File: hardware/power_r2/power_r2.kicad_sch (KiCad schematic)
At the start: 11 parts

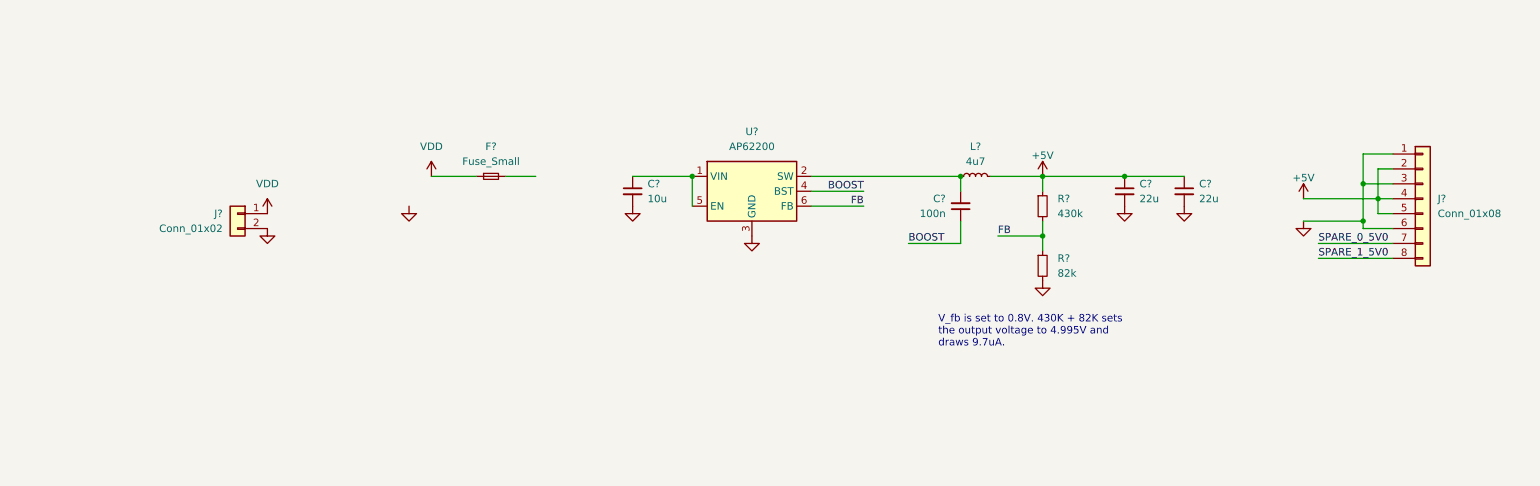
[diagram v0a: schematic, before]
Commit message: Display board layout is now 95% complete, the number of caps on the board might need some further tweaking and there are also some gaps where a few more LEDs could fit. Additionally I've decided to provide the option to use the hinges as the ground connection allowing more +5V channels on the FFC connectors which should mean more current carrying capacity. The new power board schematic has had some changes, namely the vreg has changed and so have some of the passives around it, more input protect has been added, a MOV for over voltage protection and an NMOS for reverse pol. Looking at the new vreg the power dissipation before it cooks itself (~1.1W) isn't great but it's enough for about 2.5A (at around 93% eff.) for the LEDs which hasn't usually been the bottleneck (looking at you 9V batteries). This means we're expecting around 1.8A peak input current at a Vin of 7V and need to size the fuze around that as much more current and the vreg is cooked. Might look into a over voltage shutout circuit if it seems like we're blowing fuses too often.
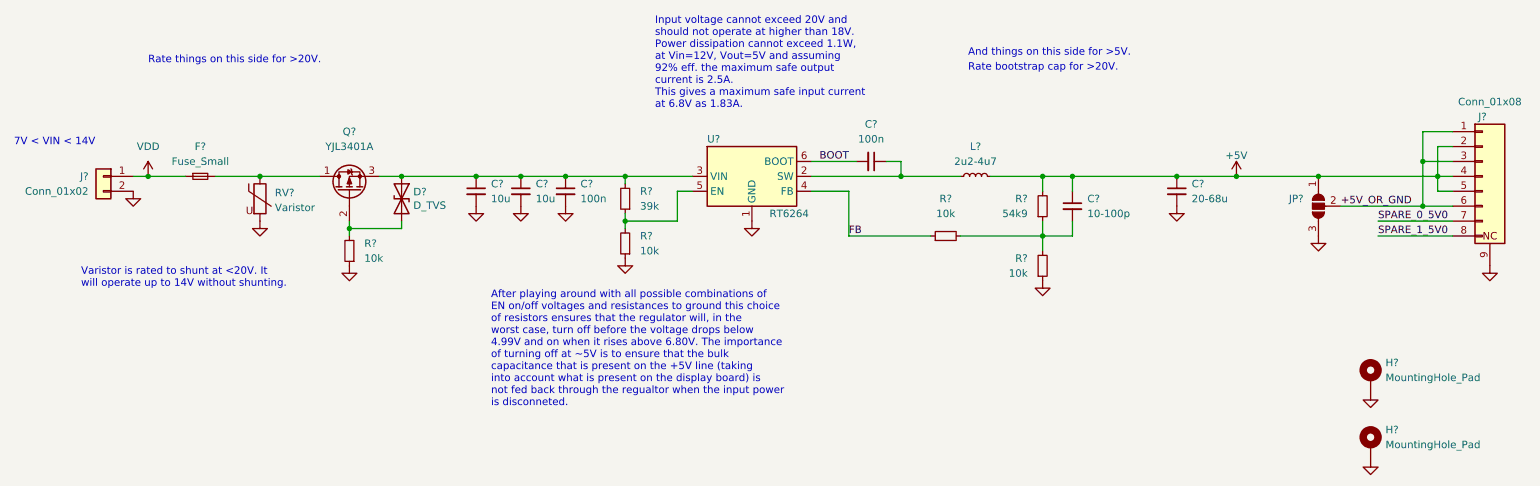
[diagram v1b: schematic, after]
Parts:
- removed C?: 22u, symbol Device:C_Small
- added C?: 10-100p, Capacitor_SMD:C_0603_1608Metric, symbol Device:C_Small
- added C? (x2): 10u, Capacitor_SMD:C_0603_1608Metric, symbol Device:C_Small
- added D?: D_TVS, Diode_SMD:D_SOD-323, symbol Device:D_TVS
- added H? (x2): MountingHole_Pad, rave_shades:M1.4 Mounting Hole, symbol Mechanical:MountingHole_Pad
- added JP?: SolderJumper_3_Open, Jumper:SolderJumper-3_P1.3mm_Open_Pad1.0x1.5mm, symbol Jumper:SolderJumper_3_Open
- added Q?: YJL3401A, symbol Device:Q_PMOS_DGS
- added R? (x3): 10k, Resistor_SMD:R_0603_1608Metric, symbol Device:R_Small
- added R?: 39k, Resistor_SMD:R_0603_1608Metric, symbol Device:R_Small
- added RV?: Varistor, symbol Device:Varistor
- C?: footprint (none) -> Capacitor_SMD:C_0603_1608Metric
- C?: value 22u -> 20-68u; footprint (none) -> Capacitor_SMD:C_0603_1608Metric
- C?: value 10u -> 100n; footprint (none) -> Capacitor_SMD:C_0603_1608Metric
- F?: Item Link (none) -> https://www.digikey.com.au/en/products/detail/bel-fuse-inc/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
- J?: footprint (none) -> rave_shades:CF35082D0RE-NH; symbol Connector_Generic:Conn_01x08 -> rave_shades:Conn_01x08
- L?: value 4u7 -> 2u2-4u7
- R?: value 430k -> 54k9; footprint (none) -> Resistor_SMD:R_0603_1608Metric
- R?: value 82k -> 10k; footprint (none) -> Resistor_SMD:R_0603_1608Metric
- U?: value AP62200 -> RT6264; footprint Package_TO_SOT_SMD:SOT-563 -> Package_TO_SOT_SMD:TSOT-23-6; symbol Regulator_Switching:AP62250Z6 -> rave_shades:RT6264; Item Link (none) -> https://www.digikey.com.au/en/products/detail/richtek-usa-i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
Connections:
- net +5V: now also R?.2, C?.1, JP?.1 (A); no longer R?.1
- net FB: now also U?.4 (FB), R?.1; no longer R?.1, R?.2, U?.6 (FB)
- net GND: now also J?.9 (NC), R?.1, U?.1 (GND), C?.2, C?.2, H?.1, H?.1, JP?.3 (B), R?.1, R?.1, RV?.2; no longer J?.1 (Pin_1), J?.3 (Pin_3), J?.6 (Pin_6), R?.2, U?.3 (GND)
- net at L?.1, U?.2 (SW): now also C?.1; no longer C?.2
- net at F?.2: now also Q?.1 (D), RV?.1
- removed net BOOST: C?.1, U?.4 (BST)
- new net: D?.2 (A2), Q?.2 (G), R?.2
- new net: C?.1, C?.1, C?.1, D?.1 (A1), Q?.3 (S), R?.2, U?.3 (VIN)
- new net: C?.2, R?.1, R?.2, R?.2
- new net: R?.1, R?.2, U?.5 (EN)
- new net +5V_OR_GND: J?.1 (Pin_1), J?.3 (Pin_3), J?.6 (Pin_6), JP?.2 (C)
- new net BOOT: C?.2, U?.6 (BOOT)
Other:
- note added: "7V < VIN < 14V"
- note added: "After playing around with all possible combinations of EN on/off voltages and resistances to ground this choice of resistors ensures that the regulator will, in the worst case, turn off before the voltage drops below 4.99V and on when it rises above 6.80V. The importance of turning off at ~5V is to ensure that the bulk capacitance that is present on the +5V line (taking into account what is prese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"
- note added: "And things on this side for >5V."
- note added: "Input voltage cannot exceed 20V and should not operate at higher than 18V. Power dissipation cannot exceed 1.1W, at Vin=12V, Vout=5V and assuming 92% eff. the maximum safe output current is 2.5A. This gives a maximum safe input current at 6.8V as 1.83A."
- note added: "Rate bootstrap cap for >20V."
- note added: "Rate things on this side for >20V."
- note added: "Varistor is rated to shunt at <20V. It will operate up to 14V without shunting."
- note removed: "V_fb is set to 0.8V. 430K + 82K sets the output voltage to 4.995V and draws 9.7uA."
- moved on the sheet: C?, F?, J?, U?

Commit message: First pass at the rev 2 power board.
Only did copper layers on the power board so far. Waiting to decide on a PCB fab house then I'll go back and make sure it's compliant (looking mostly at how close I can pack vias). Starting on the nucleo programmer shield next. Added a voltage divider to the enable pin on the 3V3 vreg on the controller board so it only switches on when there is enough input voltage for correct 3V3 output. I did this because I read somewhere that the RP2040 can power on at a lower voltage than a lot of flash chips and if that happens it gets into a weird state so I'm trying to make sure 3V3 comes on as quickly and sharply as possible.
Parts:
- removed C? (x2): 100n, Capacitor_SMD:C_0603_1608Metric, symbol Device:C_Small
- removed C?: 10-100p, Capacitor_SMD:C_0603_1608Metric, symbol Device:C_Small
- removed C?: 20-68u, Capacitor_SMD:C_0603_1608Metric, symbol Device:C_Small
- removed C? (x2): 10u, Capacitor_SMD:C_0603_1608Metric, symbol Device:C_Small
- removed L?: 2u2-4u7, symbol Device:L_Small
- removed R? (x3): 10k, Resistor_SMD:R_0603_1608Metric, symbol Device:R_Small
- removed R?: 54k9, Resistor_SMD:R_0603_1608Metric, symbol Device:R_Small
- removed R?: 39k, Resistor_SMD:R_0603_1608Metric, symbol Device:R_Small
- removed RV?: Varistor, symbol Device:Varistor
- removed U?: RT6264, Package_TO_SOT_SMD:TSOT-23-6, symbol rave_shades:RT6264
- added C101, C102, C103: 2u2 100V, Capacitor_SMD:C_1210_3225Metric, symbol Device:C_Small
- added C104, C105: 100n 100V, Capacitor_SMD:C_0402_1005Metric, symbol Device:C_Small
- added C106, C119: 100n, Capacitor_SMD:C_0402_1005Metric, symbol Device:C_Small
- added C107, C108, C109, C110, C111, C112: 22u, Capacitor_SMD:C_0805_2012Metric, symbol Device:C_Small
- added C113: 10n 5% 50V C0G/NP0, Capacitor_SMD:C_0603_1608Metric, symbol Device:C_Small
- added C114: 4u7, Capacitor_SMD:C_0402_1005Metric, symbol Device:C_Small
- added C115: 1u, Capacitor_SMD:C_0402_1005Metric, symbol Device:C_Small
- added C116: 3n9 5% 50V C0G/NP0, Capacitor_SMD:C_0603_1608Metric, symbol Device:C_Small
- added C117: 680p %5 50V C0G/NP0, Capacitor_SMD:C_0603_1608Metric, symbol Device:C_Small
- added C118: 100n 50V, Capacitor_SMD:C_0402_1005Metric, symbol Device:C_Small
- added JP102: Over Current Limit, Jumper:SolderJumper-3_P1.3mm_Open_Pad1.0x1.5mm, symbol Jumper:SolderJumper_3_Open
- added JP103: Power Save Enable, Jumper:SolderJumper-3_P1.3mm_Open_Pad1.0x1.5mm, symbol Jumper:SolderJumper_3_Open
- added JP104: Ultrasonic Enable, Jumper:SolderJumper-2_P1.3mm_Open_Pad1.0x1.5mm, symbol Jumper:SolderJumper_2_Open
- added L101: 15u, rave_shades:MPXV1D1054, symbol Device:L_Small
- added R102: 8k66 1%, Resistor_SMD:R_0402_1005Metric, symbol Device:R_Small
- added R103: 47k5 1%, Resistor_SMD:R_0402_1005Metric, symbol Device:R_Small
- added R104: 52k3 1%, Resistor_SMD:R_0402_1005Metric, symbol Device:R_Small
- added R105: 62k 1%, Resistor_SMD:R_0402_1005Metric, symbol Device:R_Small
- added R106: 3R3 1%, Resistor_SMD:R_0402_1005Metric, symbol Device:R_Small
- added R107: 10k 1%, Resistor_SMD:R_0402_1005Metric, symbol Device:R_Small
- added R108: 18k 1%, Resistor_SMD:R_0402_1005Metric, symbol Device:R_Small
- added R109, R114: 10k, Resistor_SMD:R_0402_1005Metric, symbol Device:R_Small
- added R110: 160k 1%, Resistor_SMD:R_0402_1005Metric, symbol Device:R_Small
- added R111: 390k 1%, Resistor_SMD:R_0402_1005Metric, symbol Device:R_Small
- added R112: 88k7 1%, Resistor_SMD:R_0402_1005Metric, symbol Device:R_Small
- added R113: 300k 0.5%, Resistor_SMD:R_0402_1005Metric, symbol Device:R_Small
- added RV101: MLVA06V26C100-R, Resistor_SMD:R_0603_1608Metric, symbol Device:Varistor
- added TP101: VFUSE Test Point, TestPoint:TestPoint_Pad_D1.5mm, symbol Connector:TestPoint
- added TP102: VSAFE Test Point, TestPoint:TestPoint_Pad_D1.5mm, symbol Connector:TestPoint
- added TP103: EN Test Point, TestPoint:TestPoint_Pad_D1.5mm, symbol Connector:TestPoint
- added TP104: PGOOD Test Point, TestPoint:TestPoint_Pad_D1.5mm, symbol Connector:TestPoint
- added TP105: +5V Test Point, TestPoint:TestPoint_Pad_D1.5mm, symbol Connector:TestPoint
- added U101: SIC473, rave_shades:Vishay PowerPAK MLP55-27, symbol rave_shades:SIC473
- D101: renamed from D?; value D_TVS -> ESDA17P20-1F2; Item Link https://www.digikey.com.au/en/products/detail/panjit-intern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 -> https://www.digikey.com.au/en/products/detail/stmicroelectr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
- F101: renamed from F?; value Fuse_Small -> SBF32302ASTP; footprint (none) -> Fuse:Fuse_1206_3216Metric; Item Link https://www.digikey.com.au/en/products/detail/bel-fuse-inc/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 -> https://www.digikey.com.au/en/products/detail/kamaya-inc/SB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
- H101, H102: renamed from H?; value MountingHole_Pad -> Mounting Hole
- J101: renamed from J?; value Conn_01x08 -> FPC Connector
- J102: renamed from J?; value Conn_01x02 -> Power Input; footprint (none) -> Connector_JST:JST_PH_S2B-PH-SM4-TB_1x02-1MP_P2.00mm_Horizontal; symbol Connector_Generic:Conn_01x02 -> Connector_Generic_MountingPin:Conn_01x02_MountingPin
- JP101: renamed from JP?; value SolderJumper_3_Open -> Hinge GND Enable
- Q101: renamed from Q?; value YJL3401A -> AONR21357; footprint (none) -> rave_shades:8-PowerVDFN (8-DFN-EP) (3x3mm); symbol Device:Q_PMOS_DGS -> Device:Q_PMOS_SGD; Item Link https://www.digikey.com.au/en/products/detail/yangzhou-yang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 -> https://www.digikey.com.au/en/products/detail/alpha-omega-s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
- R101: renamed from R?; footprint Resistor_SMD:R_0603_1608Metric -> Resistor_SMD:R_0402_1005Metric
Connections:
- net +5V: now also C106.1, C107.1, C108.1, C109.1, C110.1, C111.1, C112.1, C113.1, L101.2, R104.2, TP105.1
- net BOOT: now also C118.1, U101.4 (BOOT)
- net GND: now also C101.2, C102.2, C103.2, C104.2, C105.2, C106.2, C107.2, C108.2, C109.2, C110.2, C111.2, C112.2, C114.2, C115.2, C117.2, C119.2, R107.1, R108.1, R110.1, R111.1, R112.1, R113.1, R114.1, RV101.2, U101.23 (A_GND), U101.9 (P_GND); no longer J101.9 (NC)
- net VDD: now also C115.1, JP104.1 (A), R109.1, U101.26 (VDD); no longer F101.1, J102.1 (Pin_1)
- net V_FUSE: now reaches F101.2
- net V_FUSE: now also Q101.3 (D), RV101.1, TP101.1; no longer Q101.1 (D)
- net POL_CTRL: now reaches D101.2 (A2), Q101.2 (G), R101.2
- net V_SAFE: now reaches D101.1 (A1)
- net V_SAFE: now also Q101.1 (S), C101.1, C102.1, C103.1, C104.1, C105.1, R105.2, TP102.1, U101.1 (V_CIN), U101.7 (VIN); no longer Q101.3 (S)
- new net BOOT_2: C118.2, R106.1
- new net COMP: R103.2, U101.21 (COMP)
- new net COMP_2: C117.1, R103.1
- new net CURRENT_1_5A: JP102.3 (B), R111.2
- new net CURRENT_3A: JP102.1 (A), R110.2
- new net EN: R105.1, R108.2, TP103.1, U101.3 (EN)
- new net F_SW: R112.2, U101.24 (F_SW)
- new net I_LIMIT: JP102.2 (C), U101.25 (I_LIMIT)
- new net MODE: JP103.2 (C), U101.27 (MODE)
- new net PHASE: R106.2, U101.5 (PHASE)
- new net PWR_SAVE: JP103.1 (A), R113.2
- new net P_GOOD: R109.2, TP104.1, U101.2 (P_GOOD)
- new net SS: C119.1, U101.19 (SS)
- new net SW: L101.1, R102.2, U101.12 (SW)
- new net US: JP104.2 (B), U101.18 (US)
- new net VBUS: F101.1, J102.1 (Pin_1)
- new net V_DRV: C114.1, U101.16 (V_DRV)
- new net V_FB: R104.1, R107.2, U101.22 (V_FB)
- new net V_SNS: C116.2, U101.20 (V_SNS)
- new net V_SNS_2: C113.2, C116.1, R102.1
- new net ~{PWR_SAVE}: JP103.3 (B), R114.2
- no-connect marks 0 -> 5
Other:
- note added: "-10V < Vgs < -25V"
- note added: "6V < VIN < 24V"
- note added: "ESD Protection"
- note added: "Enable at ~6V."
- note added: "Following the reference design here (Fsw=300kHz)."
- note added: "Make sure to put a 100n cap close to both VIN and V_CIN."
- note added: "Over Current Protection"
- note added: "Reverse Polarity Protection"
- note added: "Rx = (Vinmax * Vout) / Prxmax Cxmin = Prxmax / (Vinmax * fsw * Vrampmax) 100mV < Vramp < 900mV Vramp = ((Vin - Vout) * Vout) / (Vin * fsw * Cx * Rx)"
- note added: "V_{in} = 24 -> I_{limit} = 1.48A V_{in} = 6 -> I_{limit} = 1.14A"
- note added: "V_{in} = 24 -> I_{limit} = 3.06A V_{in} = 6 -> I_{limit} = 2.72A"
- note added: "We have two possible current limits that we want to aim for depending on configuration. The limiting factory for power delivery at the moment is the connector between this board and the next; each conductor has a maximum rated current of 0.5A. If the hinges between the boards prove sufficiently reliable to carry our return current we can dedicate 6 of the 8 conductors for power delivery giving us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"
- note added: "We want to use the soft start feature to keep inrush current low to avoid damaging the FFC connection between this board and the display board (worst case current limit is 1.5A when not using the hinge as a GND connection). We need to be particularly careful because the capacitance on the display board can be quite large (~4.7uF per LED, ~150 LEDs). t_ss = Css * 0.8V / 5uA Irush = Vout * Cout / t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"
- note added: "With power save enabled the regulator will reduce switching frequency as the load decreases, down to a few hundred Hz. If this is problematic for the microphone the ultrasonic mode limits the switching frequency to above 20kHz. With power save disabled the switching frequency will be fixed to 300kHz."
- note removed: "7V < VIN < 14V"
- note removed: "After playing around with all possible combinations of EN on/off voltages and resistances to ground this choice of resistors ensures that the regulator will, in the worst case, turn off before the voltage drops below 4.99V and on when it rises above 6.80V. The importance of turning off at ~5V is to ensure that the bulk capacitance that is present on the +5V line (taking into account what is prese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"
- note removed: "And things on this side for >5V."
- note removed: "Input voltage cannot exceed 20V and should not operate at higher than 18V. Power dissipation cannot exceed 1.1W, at Vin=12V, Vout=5V and assuming 92% eff. the maximum safe output current is 2.5A. This gives a maximum safe input current at 6.8V as 1.83A."
- note removed: "Rate bootstrap cap for >20V."
- note removed: "Rate things on this side for >20V."
- note removed: "Varistor is rated to shunt at <20V. It will operate up to 14V without shunting."
- moved on the sheet: D101, F101, H101, H102, J101, JP101, Q101, R101

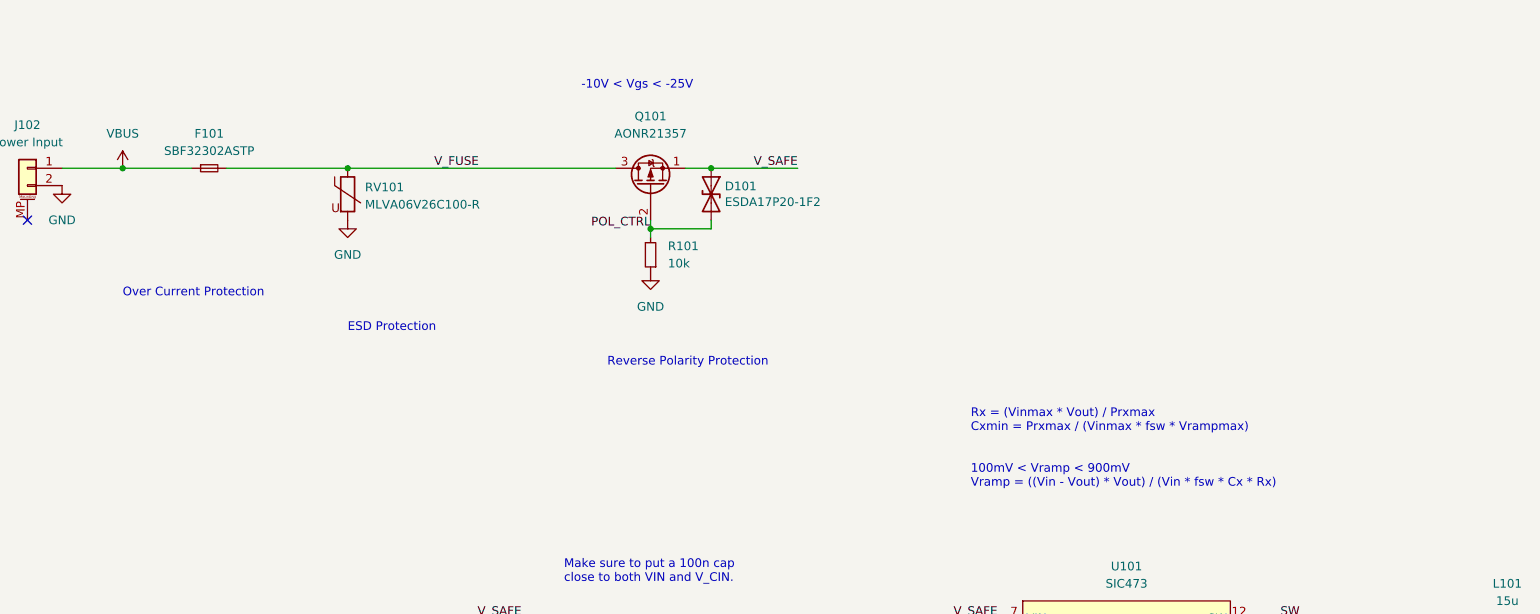
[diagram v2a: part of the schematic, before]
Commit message: Added some extra comments to the input power protection stuff.
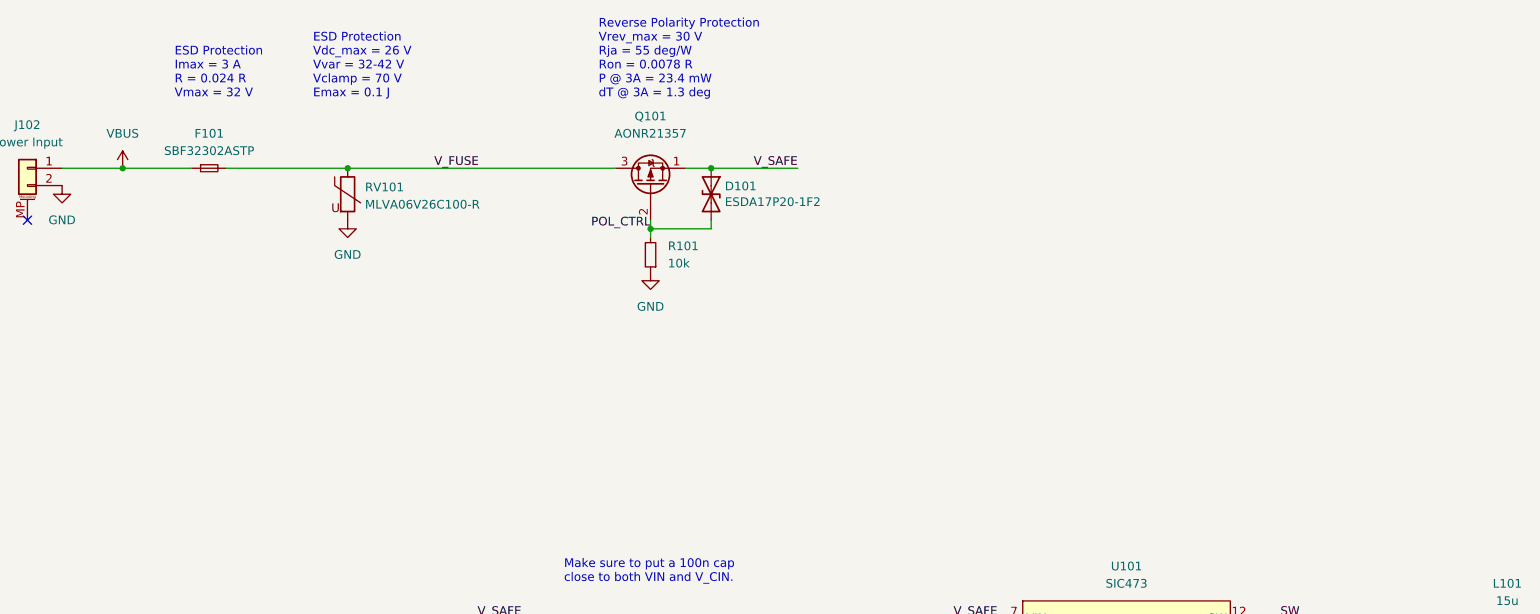
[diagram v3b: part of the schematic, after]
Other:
- note added: "ESD Protection Imax = 3 A R = 0.024 R Vmax = 32 V"
- note added: "ESD Protection Vdc_max = 26 V Vvar = 32-42 V Vclamp = 70 V Emax = 0.1 J"
- note added: "Reverse Polarity Protection Vrev_max = 30 V Rja = 55 deg/W Ron = 0.0078 R P @ 3A = 23.4 mW dT @ 3A = 1.3 deg"
- note removed: "-10V < Vgs < -25V"
- note removed: "ESD Protection"
- note removed: "Over Current Protection"
- note removed: "Reverse Polarity Protection"
- note removed: "Rx = (Vinmax * Vout) / Prxmax Cxmin = Prxmax / (Vinmax * fsw * Vrampmax) 100mV < Vramp < 900mV Vramp = ((Vin - Vout) * Vout) / (Vin * fsw * Cx * Rx)"
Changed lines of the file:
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@@
     (stroke (width 0) (type default) (color 0 0 0 0))
-  )
-  (text "-10V < Vgs < -25V" (at 121.92 26.67 0)
-    (effects (font (size 1.27 1.27)) (justify left bottom))
   )
   (text "V_{in} = 24 -> I_{limit} = 3.06A\nV_{in} = 6 -> I_{limit} = 2.72A\n"
@@
     (effects (font (size 1.27 1.27)) (justify left bottom))
   )
-  (text "Rx = (Vinmax * Vout) / Prxmax\nCxmin = Prxmax / (Vinmax * fsw * Vrampmax)\n\n\n100mV < Vramp < 900mV\nVramp = ((Vin - Vout) * Vout) / (Vin * fsw * Cx * Rx)"
-    (at 179.07 85.09 0)
-    (effects (font (size 1.27 1.27)) (justify left bottom))
-  )
   (text "6V < VIN < 24V" (at 19.05 40.64 0)
     (effects (font (size 1.27 1.27)) (justify left bottom))
   )
-  (text "Reverse Polarity Protection" (at 125.73 67.31 0)
+  (text "Reverse Polarity Protection\nVrev_max = 30 V\nRja = 55 deg/W\nRon = 0.0078 R\nP @ 3A = 23.4 mW\ndT @ 3A = 1.3 deg"
+    (at 124.46 27.94 0)
     (effects (font (size 1.27 1.27)) (justify left bottom))
   )
@@
     (effects (font (size 1.27 1.27)) (justify left bottom))
   )
-  (text "Over Current Protection" (at 54.61 57.15 0)
+  (text "ESD Protection\nVdc_max = 26 V\nVvar = 32-42 V\nVclamp = 70 V\nEmax = 0.1 J"
+    (at 82.55 27.94 0)
     (effects (font (size 1.27 1.27)) (justify left bottom))
   )
@@
     (effects (font (size 1.27 1.27)) (justify left bottom))
   )
-  (text "ESD Protection" (at 87.63 62.23 0)
+  (text "ESD Protection\nImax = 3 A\nR = 0.024 R\nVmax = 32 V\n"
+    (at 62.23 27.94 0)
     (effects (font (size 1.27 1.27)) (justify left bottom))
   )
@@
       (effects (font (size 1.27 1.27)) hide)
     )
-    (property "Datasheet" "~" (id 3) (at 132.08 40.64 0)
+    (property "Datasheet" "www.aosmd.com/res/data_sheets/AONR21357.pdf" (id 3) (at 132.08 40.64 0)
       (effects (font (size 1.27 1.27)) hide)
     )
@@
       (effects (font (size 1.27 1.27)) hide)
     )
-    (property "Datasheet" "file:///D:/Users/edenb/Downloads/esda17p20-1f2.pdf" (id 3) (at 140.97 41.91 0)
-      (effects (font (size 1.27 1.27)) hide)
-    )
-    (property "Description" "" (id 4) (at 46.99 -45.72 0)
-      (effects (font (size 1.27 1.27)) hide)
-    )
+    (property "Datasheet" "https://www.st.com/resource/en/datasheet/esda17p20-1f2.pdf" (id 3) (at 140.97 41.91 0)
+      (effects (font (size 1.27 1.27)) hide)
+    )
